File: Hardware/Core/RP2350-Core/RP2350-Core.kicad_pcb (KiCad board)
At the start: 2 copper layers, 66.8 x 66.2 mm, 89 parts, among them CN10 PR5L4015-5P-C-F, CN11 PR5L4015-5P-C-F, CN7 PR5L4015-5P-C-F, CN8 PR5L4015-5P-C-F, CN9 PR5L4015-5P-C-F, J2 Conn_02x05_Counter_Clockwise, J4 Conn_02x05_Counter_Clockwise, J5 Conn_02x05_Counter_Clockwise, J7 SWD, Q2 2N7002, Q3 2N7002, SW1 TS-1187A-B-A-B, SW2 TS-1187A-B-A-B, U19 W25Q16JVSNIQ, U2 AP2112K-3.3, U3 LM66200DRLR, U35 PR5L5015-5P-C-H, U36 PR5L5015-5P-C-H, U37 PR5L5015-5P-C-H, U38 PR5L5015-5P-C-H, U39 PR5L5015-5P-C-H, U4 RP2350A, Y1 Crystal

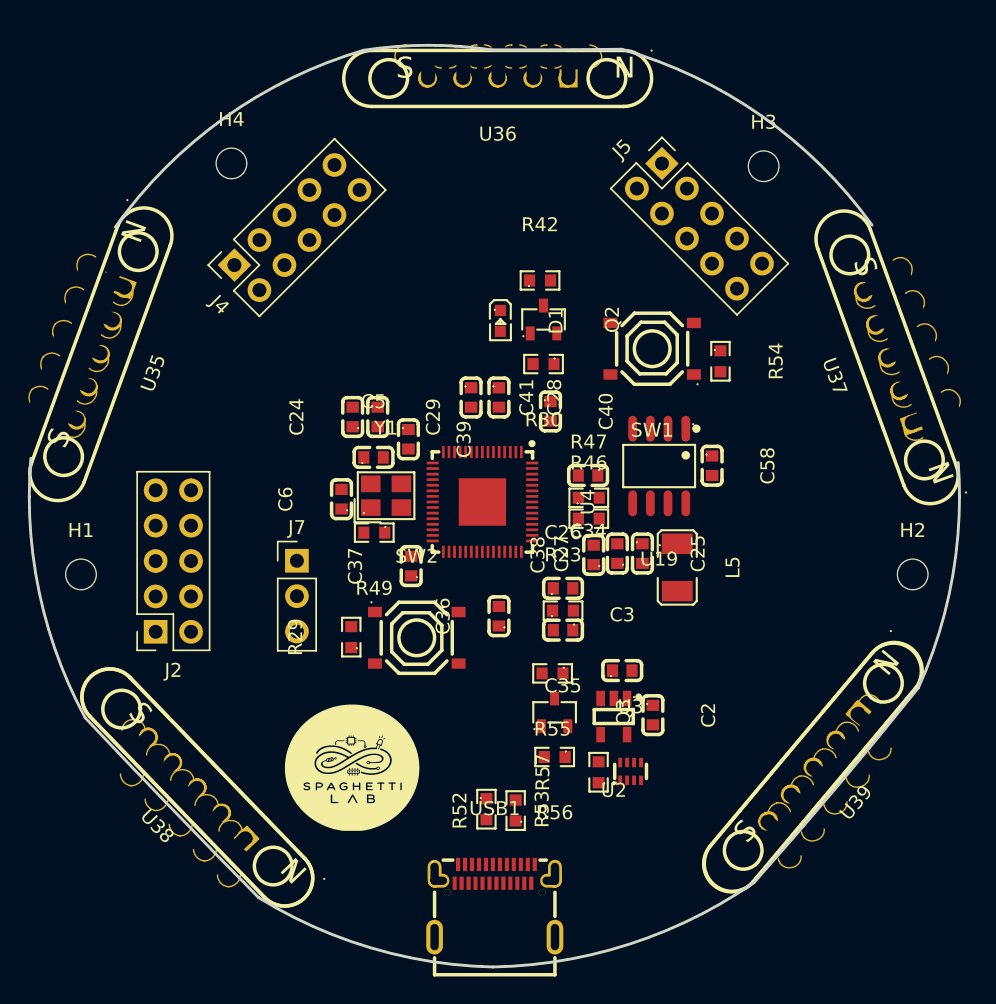
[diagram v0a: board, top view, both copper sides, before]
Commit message: Routing core started
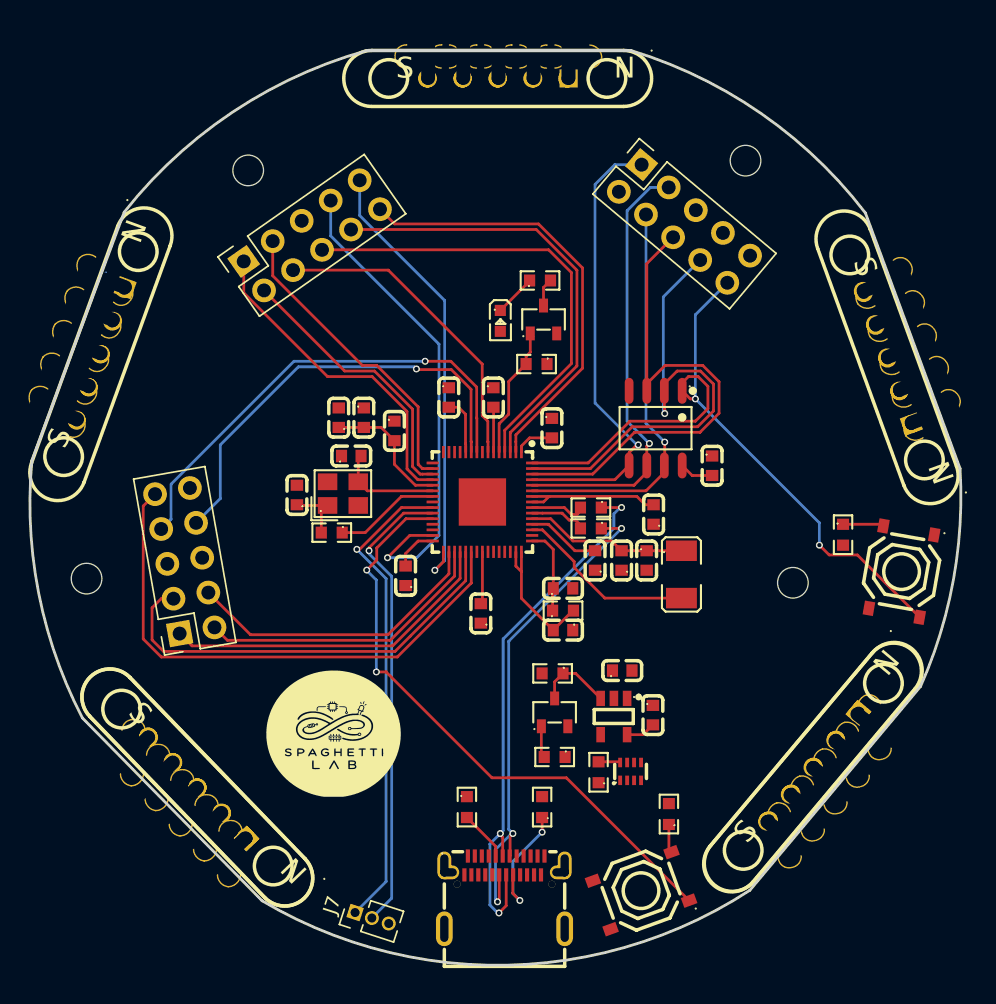
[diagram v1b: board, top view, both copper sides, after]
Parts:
- J7: footprint Connector_PinHeader_2.54mm:PinHeader_1x03_P2.54mm_Vertical -> Connector_PinHeader_1.27mm:PinHeader_1x03_P1.27mm_Vertical
- moved R29 26.1 mm to (97.9, 92.0)
- moved J7 25.6 mm to (75.4, 99.1), turned to 72 degrees
- moved SW2 24.3 mm to (95.9, 97.5), turned to -160 degrees
- moved SW1 24.0 mm to (114.6, 74.6), turned to -100 degrees
- moved R54 15.2 mm to (110.4, 72.0)
- moved H2 8.62 mm to (106.8, 75.4)
- moved C34 5.47 mm to (96.8, 70.5), turned to 90 degrees
- moved C6 3.21 mm to (71.2, 69.1)
- moved Y1 3.10 mm to (74.5, 69.0)
- moved R49 3.05 mm to (73.7, 71.8)
- moved U19 2.73 mm to (96.9, 64.3)
- moved R47 2.21 mm to (92.3, 71.5), turned to 180 degrees
- moved R52 1.92 mm to (88.8, 91.5)
- moved J2 1.73 mm to (62.8, 79.0), turned to -170 degrees
- moved C5 1.60 mm to (75.1, 66.3)
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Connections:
- J2 pad 1: /InOut (page 4)/GPIO20 -> /InOut (page 4)/GPIO22
- J2 pad 3: /InOut (page 4)/GPIO22 -> /InOut (page 4)/GPIO23
- J2 pad 4: /InOut (page 4)/GPIO23 -> /InOut (page 4)/GPIO20
- J4 pad 1: /InOut (page 4)/GPIO1 -> /InOut (page 4)/GPIO15
- J4 pad 10: /InOut (page 4)/GPIO13 -> /InOut (page 4)/GPIO0
- J4 pad 2: /InOut (page 4)/GPIO0 -> /InOut (page 4)/GPIO14
- J4 pad 3: /InOut (page 4)/GPIO2 -> /InOut (page 4)/GPIO13
- J4 pad 6: /InOut (page 4)/GPIO19 -> /InOut (page 4)/GPIO2
- J4 pad 8: /InOut (page 4)/GPIO15 -> /InOut (page 4)/GPIO1
- J4 pad 9: /InOut (page 4)/GPIO14 -> /InOut (page 4)/GPIO19
- J5 pad 1: /InOut (page 4)/QSPI_SD3 -> /InOut (page 4)/QSPI_SD0
- J5 pad 2: /InOut (page 4)/QSPI_SD2 -> GND
- J5 pad 3: /InOut (page 4)/QSPI_SD1 -> /InOut (page 4)/QSPI_SCLK
- J5 pad 4: /InOut (page 4)/QSPI_SD0 -> /InOut (page 4)/QSPI_SD3
- J5 pad 5: /InOut (page 4)/QSPI_SCLK -> GND
- J5 pad 6: GND -> /InOut (page 4)/QSPI_SD2
- J5 pad 8: GND -> /InOut (page 4)/QSPI_SD1
- U4 pad 13: /Logic/ID -> /InOut (page 4)/ID
- USB1 pad A1: unconnected-(USB1-GND-PadA1) -> GND
- USB1 pad A12: unconnected-(USB1-GND-PadA12) -> GND
- USB1 pad B1: unconnected-(USB1-GND-PadB1) -> GND
- USB1 pad B12: unconnected-(USB1-GND-PadB12) -> GND
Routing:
- net /InOut (page 4)/QSPI_SS: track 0.00 -> 53.4 mm, vias 0 -> 2
- net +3V3: track 0.00 -> 51.4 mm
- net /Logic/~{RESET}: track 0.00 -> 43.6 mm, vias 0 -> 2
- net /Logic/USB_DP: track 0.00 -> 39.6 mm, vias 0 -> 3
- net /InOut (page 4)/GPIO24: track 0.00 -> 39.3 mm
- net /InOut (page 4)/QSPI_SD2: track 0.00 -> 36.5 mm
- net /Logic/USB_DM: track 0.00 -> 35.8 mm, vias 0 -> 3
- net /InOut (page 4)/GPIO18: track 0.00 -> 35.5 mm, vias 0 -> 1
- net /InOut (page 4)/QSPI_SD1: track 0.00 -> 35.5 mm, vias 0 -> 1
- net /Logic/SWC: track 0.00 -> 34.5 mm, vias 0 -> 1
- net /InOut (page 4)/SDA_ALT: track 0.00 -> 34.5 mm, vias 0 -> 1
- net /InOut (page 4)/GPIO2: track 0.00 -> 33.4 mm
- net /Logic/SIO: track 0.00 -> 33.4 mm, vias 0 -> 1
- net /InOut (page 4)/QSPI_SD0: track 0.00 -> 33.2 mm, vias 0 -> 1
- net /InOut (page 4)/GPIO1: track 0.00 -> 32.5 mm
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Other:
- board size 66.8 x 66.2 mm -> 66.8 x 65.6 mm

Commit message: RP235X Layout complete
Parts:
- removed the U38 at (64.1, 90.1)
- removed the U39 at (108.2, 88.7)
- moved ? 810.1 mm to (900.7, 27.6)
- moved ? 10.0 mm to (88.2, 27.6)
- moved ? 10.0 mm to (66.4, 104.8)
- moved ? 10.0 mm to (59.4, 97.6)
- moved ? 10.0 mm to (44.8, 60.7)
- moved ? 10.0 mm to (119.5, 89.6)
- moved ? 10.0 mm to (122.6, 85.8)
- moved ? 10.0 mm to (46.5, 56.0)
- moved ? 10.0 mm to (61.2, 99.4)
- moved ? 10.0 mm to (116.2, 93.5)
- moved ? 10.0 mm to (64.7, 103.0)
- moved ? 10.0 mm to (123.3, 53.9)
- moved ? 10.0 mm to (62.9, 101.2)
- moved ? 10.0 mm to (125.1, 58.7)
- moved ? 10.0 mm to (85.7, 27.6)
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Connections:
- CN9 pad 3: /Logic/~{RESET} -> /InOut (page 4)/~{RESET}
- SW2 pad 1: /Logic/~{RESET} -> Net-(SW2-A)
- U36 pad 3: /Logic/~{RESET} -> /InOut (page 4)/~{RESET}
- U4 pad 12: /Logic/~{RESET} -> /InOut (page 4)/~{RESET}
- U4 pad 26: /Logic/~{RESET} -> Net-(SW2-A)
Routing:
- net GND: track 0.00 -> 51.6 mm, vias 0 -> 44
- net /InOut (page 4)/FLEX5: track 0.00 -> 47.4 mm, vias 0 -> 1
- net /InOut (page 4)/FLEX6: track 0.00 -> 46.3 mm, vias 0 -> 2
- net Net-(SW2-A): track 0.00 -> 44.1 mm, vias 0 -> 2
- net /Logic/~{RESET}: track 43.6 -> 0.00 mm, vias 2 -> 0
- net /InOut (page 4)/FLEX0: track 0.00 -> 41.4 mm, vias 0 -> 2
- net /InOut (page 4)/FLEX1: track 0.00 -> 41.1 mm, vias 0 -> 2
- net /InOut (page 4)/ID: track 0.00 -> 40.7 mm, vias 0 -> 2
- net +3V3: track 51.4 -> 88.8 mm, vias 0 -> 9
- net /InOut (page 4)/FLEX4: track 0.00 -> 31.1 mm, vias 0 -> 1
- net /InOut (page 4)/FLEX3: track 0.00 -> 30.1 mm, vias 0 -> 1
- net /InOut (page 4)/SCL_AUX: track 0.00 -> 30.0 mm, vias 0 -> 2
- net /InOut (page 4)/FLEX2: track 0.00 -> 29.9 mm, vias 0 -> 1
- net /InOut (page 4)/SDA_AUX: track 0.00 -> 29.7 mm, vias 0 -> 2
- net /InOut (page 4)/~{INT}: track 0.00 -> 28.3 mm, vias 0 -> 1
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- added copper zone on In2.Cu, net +3V3
- added copper zone on In2.Cu, net /Logic/VBUS
- added copper zone on F.Cu, net GND
- added copper zone on In1.Cu, net GND
- added copper zone on In2.Cu, net VLOGIC
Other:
- copper layers 2 -> 4

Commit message: completed RP235x pogo review
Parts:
- removed the ? at (66.4, 104.8)
- removed the ? at (59.4, 97.6)
- removed the ? at (44.8, 60.7)
- removed the ? at (119.5, 89.6)
- removed the ? at (122.6, 85.8)
- removed the ? at (46.5, 56.0)
- removed the ? at (61.2, 99.4)
- removed the ? at (116.2, 93.5)
- removed the ? at (64.7, 103.0)
- removed the ? at (123.3, 53.9)
- removed the ? at (62.9, 101.2)
- removed the ? at (125.1, 58.7)
- removed the ? at (85.7, 27.6)
- removed the ? at (80.6, 27.6)
- removed the ? at (83.1, 27.6)
- removed the ? at (47.4, 53.6)
- removed the ? at (45.7, 58.4)
- removed the ? at (121.1, 87.7)
- removed the ? at (44.0, 63.1)
- removed the ? at (126.8, 63.4)
- removed the ? at (117.8, 91.6)
- removed the ? at (124.2, 56.3)
- removed the ? at (88.2, 27.6)
- removed the ? at (125.9, 61.0)
- added ?: , , F.Cu at (116.8, 63.4)
- added ?: , , F.Cu at (112.6, 85.8)
- added ?: , , F.Cu at (59.4, 87.6)
- added ?: , , F.Cu at (90.7, 37.6)
- added ?: , , F.Cu at (113.3, 53.9)
- added ?: , , F.Cu at (54.0, 63.1)
- added ?: , , F.Cu at (55.7, 58.4)
- added ?: , , F.Cu at (66.4, 94.8)
- added ?: , , F.Cu at (115.9, 61.0)
- added ?: , , F.Cu at (115.1, 58.7)
- added ?: , , F.Cu at (64.7, 93.0)
- added ?: , , F.Cu at (57.4, 53.6)
- added ?: , , F.Cu at (106.2, 93.5)
- added ?: , , F.Cu at (109.5, 89.6)
- added ?: , , F.Cu at (111.1, 87.7)
- added ?: , , F.Cu at (83.1, 37.6)
- added ?: , , F.Cu at (56.5, 56.0)
- added ?: , , F.Cu at (54.8, 60.7)
- added ?: , , F.Cu at (85.7, 37.7)
- added ?: , , F.Cu at (114.2, 56.3)
- added ?: , , F.Cu at (62.9, 91.2)
- added ?: , , F.Cu at (88.2, 37.7)
- added ?: , , F.Cu at (107.8, 91.6)
- added ?: , , F.Cu at (80.6, 37.6)
- added ?: , , F.Cu at (61.2, 89.4)
- moved R54 2.45 mm to (108.5, 70.4), turned to 180 degrees
- moved C40 0.42 mm to (89.9, 64.3)
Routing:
- net /Logic/USB_DM: track 35.8 -> 43.5 mm
- net /Logic/SIO: track 34.1 -> 38.1 mm
- net /Logic/SWC: track 34.9 -> 38.9 mm
- net Net-(SW1-C): track 2.95 -> 4.43 mm
- net /InOut (page 4)/ID: track 40.7 -> 41.6 mm
- net /InOut (page 4)/GPIO18: track 32.9 -> 32.3 mm
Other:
- board text added: "+5V"
- board text added: "BOOTSEL"
- board text added: "CORE"
- board text added: "FLEX2"
- board text added: "FLEX3"
- board text added: "FLEX4"
- board text added: "FLEX5"
- board text added: "FLEX6"
- board text added: "GND"
- board text added: "MCU"
- board text added: "MODULE"
- board text added: "RESET"
- board text added: "RP235x"
- board text added: "SCL_AUX"
- board text added: "SDA_AUX"
- board text added: "SIO"
- board text added: "SWC"
- board text added: "VEXT"
- board text added: "VHV"
- board text added: "VLOGIC"
- board text added: "~{INT}"
- board text added: "~{RESET}"

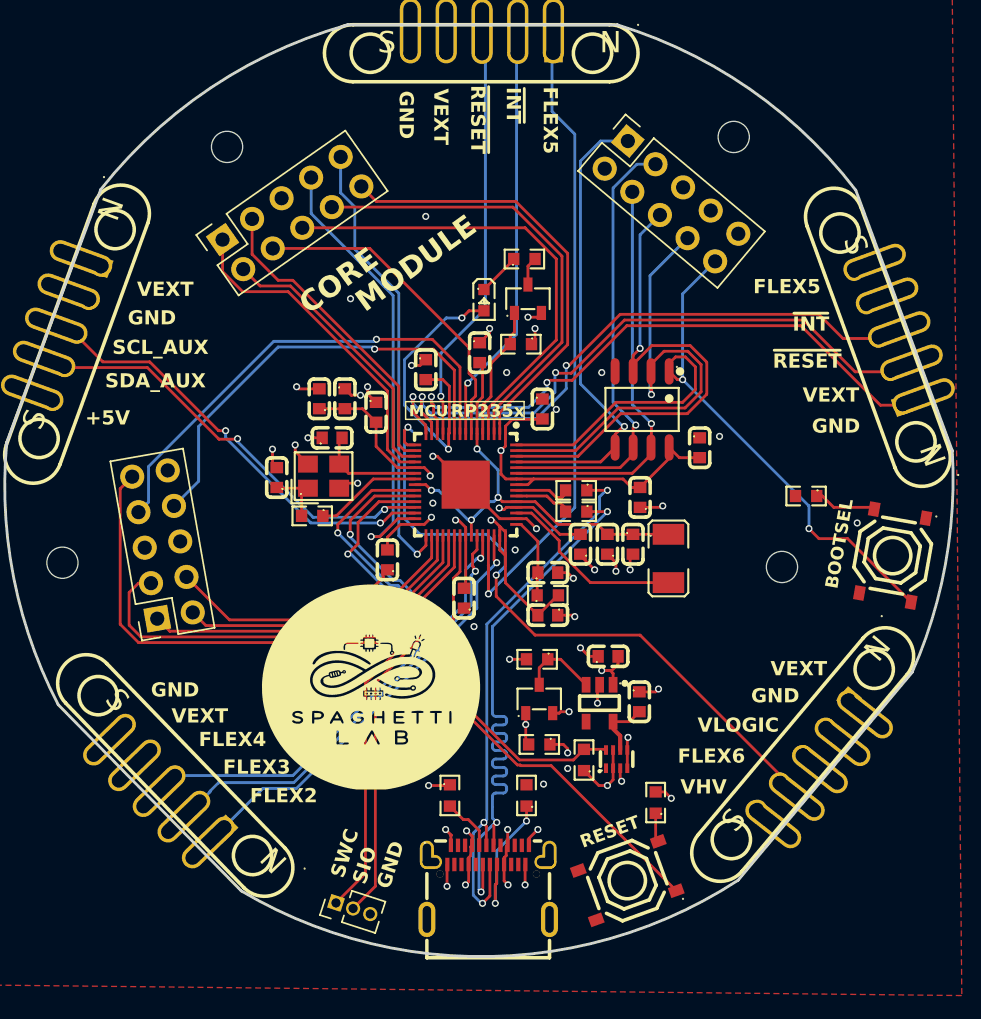
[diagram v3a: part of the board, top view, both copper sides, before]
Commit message: Added labels on the board
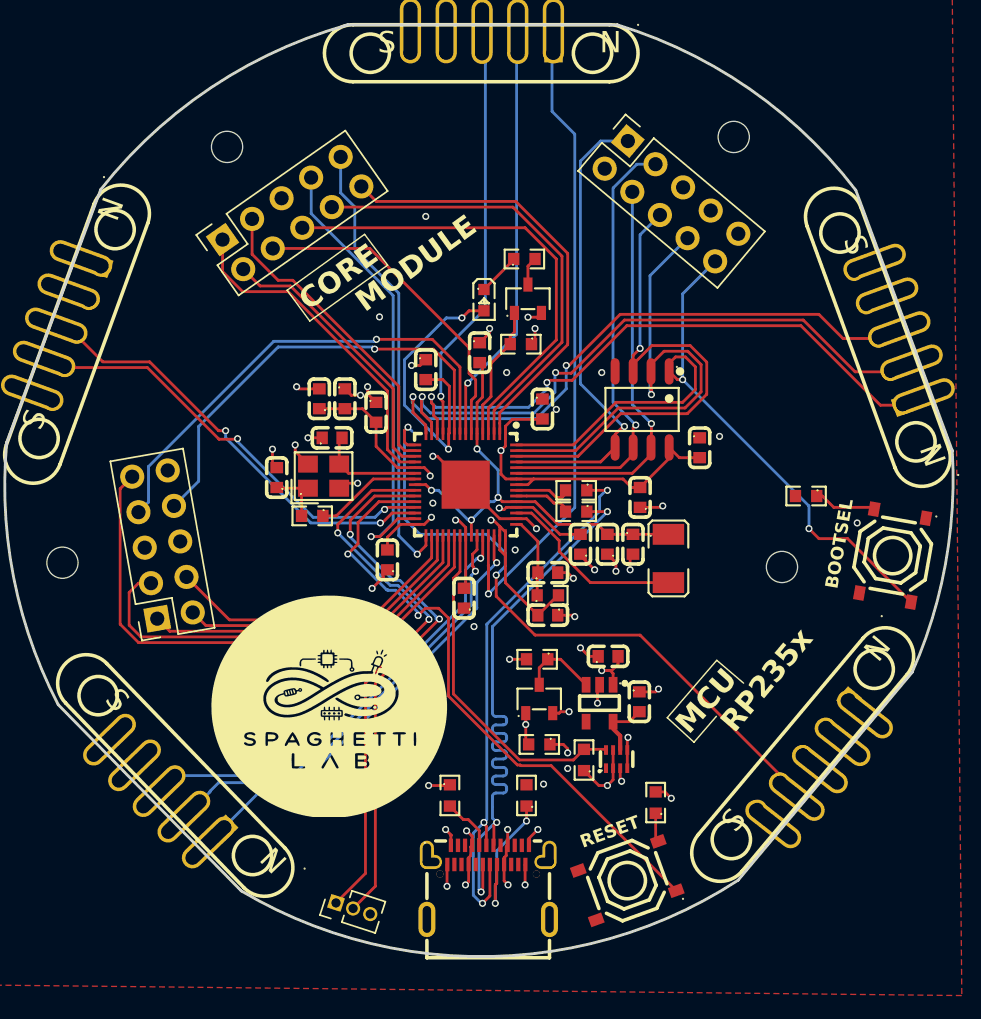
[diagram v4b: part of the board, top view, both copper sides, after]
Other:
- board text added: "+3V3"
- board text added: "FLEX0"
- board text added: "FLEX1"
- board text added: "GPIO0"
- board text added: "GPIO1"
- board text added: "GPIO13"
- board text added: "GPIO14"
- board text added: "GPIO15"
- board text added: "GPIO18"
- board text added: "GPIO19"
- board text added: "GPIO2"
- board text added: "GPIO20"
- board text added: "GPIO21"
- board text added: "GPIO22"
- board text added: "GPIO23"
- board text added: "GPIO24"
- board text added: "GPIO4"
- board text added: "ID"
- board text added: "QSPI_SCLK"
- board text added: "QSPI_SD0"
- board text added: "QSPI_SD1"
- board text added: "QSPI_SD2"
- board text added: "QSPI_SD3"
- board text added: "QSPI_SS"
- board text added: "SCL_ALT"
- board text added: "SDA_ALT"
- board text removed: "FLEX3"

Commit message: Resolved DRC
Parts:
- removed the ? at (900.7, 27.6)
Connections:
- ? pad 3: RESET_N -> /InOut (page 4)/~{RESET}
- ? pad 3: INT_N -> /InOut (page 4)/~{INT}
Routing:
- net +3V3: track 89.2 -> 90.9 mm
- net GND: track 51.9 -> 52.9 mm
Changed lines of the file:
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@@
 		(capping no)
 		(filling no)
+		(zone_defaults)
 		(pcbplotparams
 			(layerselection 0x00000000_00000000_55555555_5755f5ff)
@@
 			(layers "*.Cu" "*.Mask")
 			(remove_unused_layers no)
-			(net "RESET_N")
+			(net "/InOut (page 4)/~{RESET}")
 			(pinfunction "VEXT")
 			(pintype "unspecified")
@@
 			(layers "*.Cu" "*.Mask")
 			(remove_unused_layers no)
-			(net "INT_N")
+			(net "/InOut (page 4)/~{INT}")
 			(pinfunction "VEXT")
 			(pintype "unspecified")
@@
 		(embedded_fonts no)
 	)
-	(footprint "Pad_e175"
-		(layer "F.Cu")
-		(at 900.695437 27.629996 -90)
-		(property "Reference" ""
-			(at 0 0 270)
-			(layer "F.SilkS")
-			(hide yes)
-			(effects
-				(font
-					(size 1.27 1.27)
-				)
-			)
-		)
-		(property "Value" ""
-			(at 0 0 270)
-			(layer "F.Fab")
-			(effects
-				(font
-					(size 1.27 1.27)
-				)
-			)
-		)
-		(property "Datasheet" ""
-			(at 0 0 270)
-			(layer "F.Fab")
-			(hide yes)
-			(effects
-				(font
-					(size 1.27 1.27)
-				)
-			)
-		)
-		(property "Description" ""
-			(at 0 0 270)
-			(layer "F.Fab")
-			(hide yes)
-			(effects
-				(font
-					(size 1.27 1.27)
-				)
-			)
-		)
-		(duplicate_pad_numbers_are_jumpers no)
-		(pad "62" thru_hole custom
-			(at 0 0 270)
-			(size 0.000001 0.000001)
-			(drill oval 4.1 1)
-			(layers "*.Cu" "*.Mask")
-			(remove_unused_layers no)
-			(net "FLEX5")
-			(thermal_bridge_angle 90)
-			(options
-				(clearance outline)
-				(anchor circle)
-			)
-			(primitives
-				(gr_poly
-					(pts
-						(xy -0.8275 1.593) (xy -0.828 1.5665) (xy -0.8275 1.5535) (xy -0.828 1.55)
-					)
-					(width 0)
-					(fill yes)
-				)
-				(gr_arc
-					(start -0.8275 1.536)
-					(mid -0.827422 1.543012)
-					(end -0.828 1.55)
-					(width 0.1)
-				)
-				(gr_arc
-					(start -0.8275 -1.5265)
-					(mid -0.561023 -2.112662)
-					(end 0.026 -2.3775)
-					(width 0.1)
-				)
-				(gr_arc
-					(start 0.026 -2.3775)
-					(mid 0.588707 -2.107778)
-					(end 0.828 -1.5315)
-					(width 0.1)
-				)
-				(gr_arc
-					(start 0.828 1.5815)
-					(mid 0.603315 2.14077)
-					(end 0.048 2.3755)
-					(width 0.1)
-				)
-				(gr_poly
-					(pts
-						(xy 0.048 2.3755) (xy 0.0485 2.375) (xy -0.022 2.3765) (xy -0.0215 2.3765)
-					)
-					(width 0)
-					(fill yes)
-				)
-				(gr_arc
-					(start -0.0215 2.3765)
-					(mid -0.593579 2.158489)
-					(end -0.8275 1.593)
-					(width 0.1)
-				)
-			)
-		)
-		(embedded_fonts no)
-	)
 	(footprint ""
 		(layer "F.Cu")
@@
 	(gr_line
 		(start 76.2 37.2)
-		(end 95.2 37.2)
+		(end 95.199986 37.2)
 		(stroke
 			(width 0.2)
@@
 	)
 	(segment
+		(start 92.07 76.17)
+		(end 91.7 75.8)
+		(width 0.2)
+		(layer "F.Cu")
+		(net "GND")
+	)
+	(segment
 		(start 74.2 62.85)
 		(end 72.75 62.85)
@@
 	)
 	(segment
-		(start 91.7 75.8)
-		(end 92.1 76.2)
-		(width 0.2)
-		(layer "F.Cu")
-		(net "GND")
-	)
-	(segment
 		(start 88.8 72)
 		(end 88.08375 72)
@@
 	)
 	(segment
+		(start 92.07 77.01)
+		(end 92.07 76.17)
+		(width 0.2)
+		(layer "F.Cu")
+		(net "GND")
+	)
+	(segment
 		(start 78.7 75.9)
 		(end 79 75.6)
@@
 	)
 	(segment
-		(start 91 75.8)
-		(end 91.7 75.8)
-		(width 0.2)
-		(layer "F.Cu")
-		(net "GND")
-	)
-	(segment
 		(start 95.9 87.457864)
 		(end 95.95 87.407864)
@@
 	)
 	(segment
+		(start 91.95 77.13)
+		(end 92.07 77.01)
+		(width 0.2)
+		(layer "F.Cu")
+		(net "GND")
+	)
+	(segment
 		(start 83.1 93.9)
 		(end 83.5 94.3)
@@
 		(net "GND")
 	)
+	(segment
+		(start 91.7 75.8)
+		(end 91 75.8)
+		(width 0.2)
+		(layer "F.Cu")
+		(net "GND")
+	)
 	(via
 		(at 95.95 87.407864)
@@
 	)
 	(via
-		(at 92.1 76.2)
+		(at 91.95 77.13)
 		(size 0.5)
 		(drill 0.3)
@@
 	)
 	(segment
+		(start 65.272823 68.597177)
+		(end 65.28 68.59)
+		(width 0.2)
+		(layer "In2.Cu")
+		(net "+3V3")
+	)
+	(segment
+		(start 63.517867 68.597177)
+		(end 65.272823 68.597177)
+		(width 1.5)
+		(layer "In2.Cu")
+		(net "+3V3")
+	)
+	(segment
 		(start 85.7 63.434314)
 		(end 85.7 61.2)
@@
 	)
 	(segment
-		(start 86.1 75.3)
-		(end 86.11375 75.31375)
-		(width 0.2)
-		(layer "F.Cu")
-		(net "/InOut (page 4)/FLEX5")
-	)
-	(segment
 		(start 86.11375 73.18)
 		(end 86.11375 77.3)
@@
 		(width 0.2)
 		(layer "B.Cu")
-		(net "/InOut (page 4)/FLEX6")
-	)
-	(segment
-		(start 80.45 65.55)
-		(end 80.75 65.85)
-		(width 0.2)
-		(layer "B.Cu")
